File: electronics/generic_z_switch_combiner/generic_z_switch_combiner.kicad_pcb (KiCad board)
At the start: 2 copper layers, 18 x 14.5 mm, 7 parts, among them J1 Conn_01x02, J2 Conn_01x02, J3 Conn_01x02

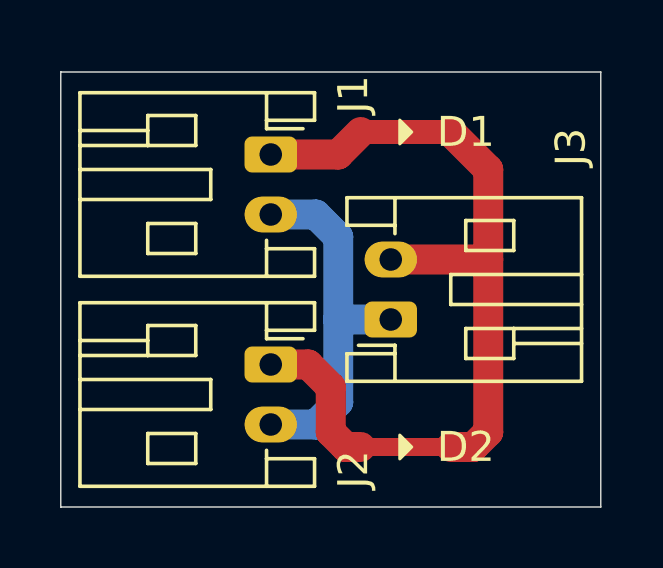
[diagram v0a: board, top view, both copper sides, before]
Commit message: rotated diodes around to something more logical
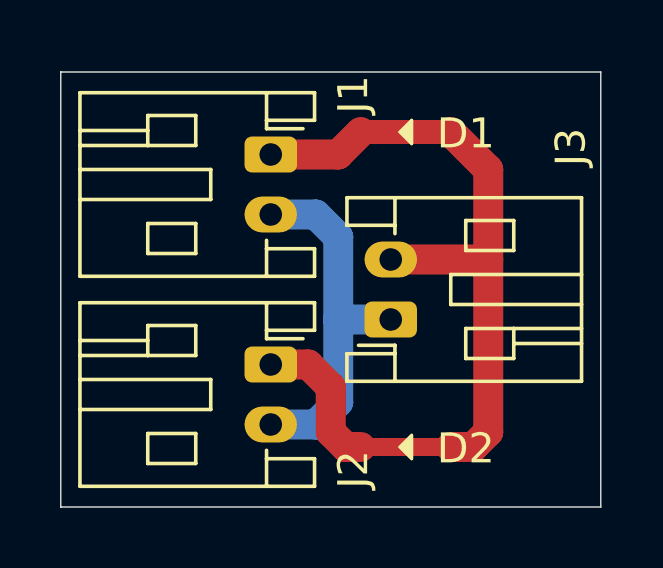
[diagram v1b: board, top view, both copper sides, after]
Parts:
- turned D1 to 0 degrees
- turned D2 to 0 degrees
